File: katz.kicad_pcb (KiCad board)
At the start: 2 copper layers, 184.5 x 68.8 mm, 62 parts, among them SW1 choc_SW_HS, SW10 choc_SW_HS, SW11 choc_SW_HS, SW12 choc_SW_HS, SW13 choc_SW_HS, SW14 choc_SW_HS, SW15 choc_SW_HS, SW16 choc_SW_HS, SW17 choc_SW_HS, SW18 choc_SW_HS, SW19 choc_SW_HS, SW2 choc_SW_HS, SW20 choc_SW_HS, SW21 choc_SW_HS, SW22 choc_SW_HS, SW23 choc_SW_HS, SW24 choc_SW_HS, SW25 choc_SW_HS, SW26 choc_SW_HS, SW27 choc_SW_HS, SW28 choc_SW_HS, SW29 choc_SW_HS, SW3 choc_SW_HS, SW30 choc_SW_HS, SW4 choc_SW_HS, SW5 choc_SW_HS, SW6 choc_SW_HS, SW7 choc_SW_HS, SW8 choc_SW_HS, SW9 choc_SW_HS, U1 SeeeduinoXIAO

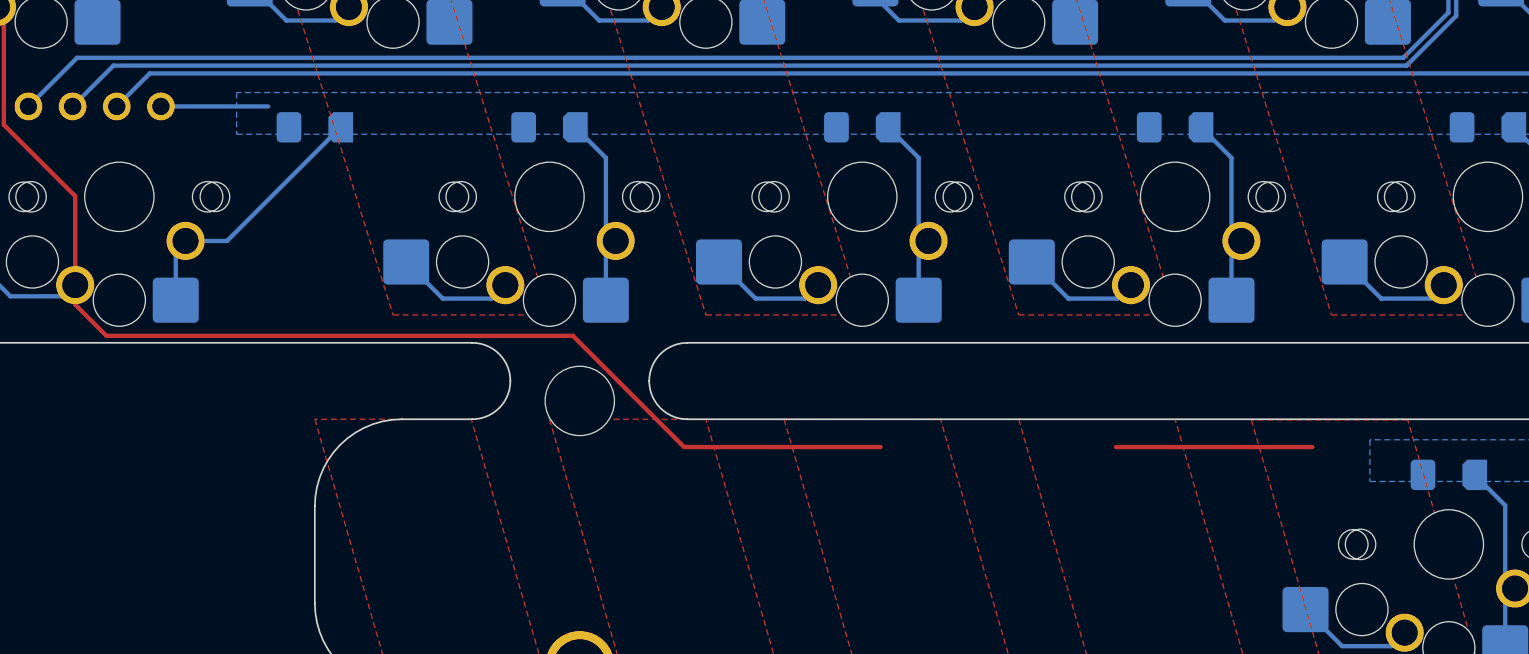
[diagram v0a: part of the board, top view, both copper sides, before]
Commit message: add pins to removable space bar
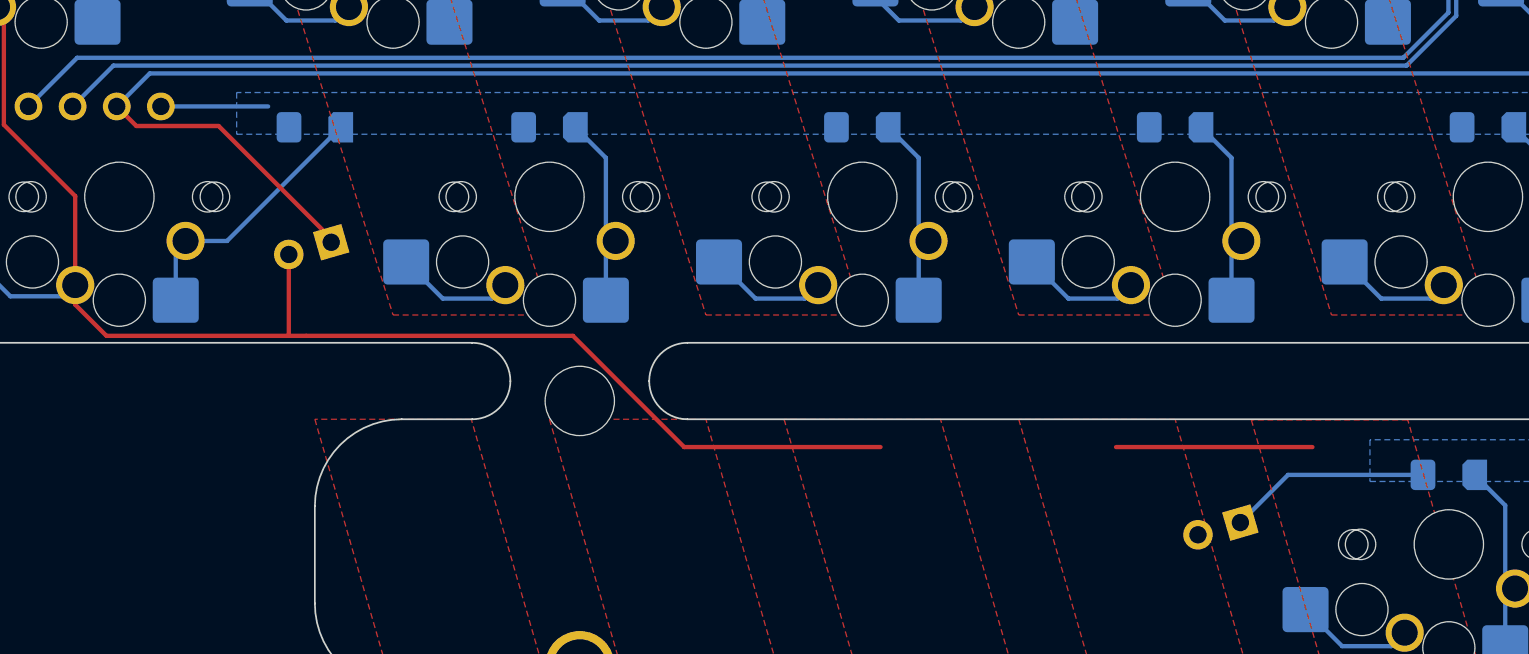
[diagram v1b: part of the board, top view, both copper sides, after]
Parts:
- added J1: modular spacebar, Connector_PinHeader_2.54mm:PinHeader_2x01_P2.54mm_Vertical, F.Cu at (129.8, 114.7)
- added J2: connector for modular spacebar, Connector_PinHeader_2.54mm:PinHeader_2x01_P2.54mm_Vertical, F.Cu at (77.4, 98.6)
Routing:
- net r6: track 117.0 -> 144.3 mm
- net c1: track 327.2 -> 331.9 mm

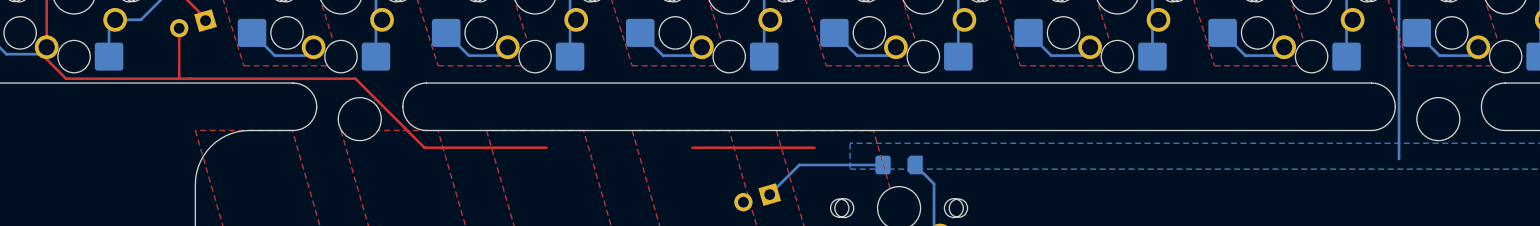
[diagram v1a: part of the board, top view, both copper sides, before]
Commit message: add break-off cuts to space bar
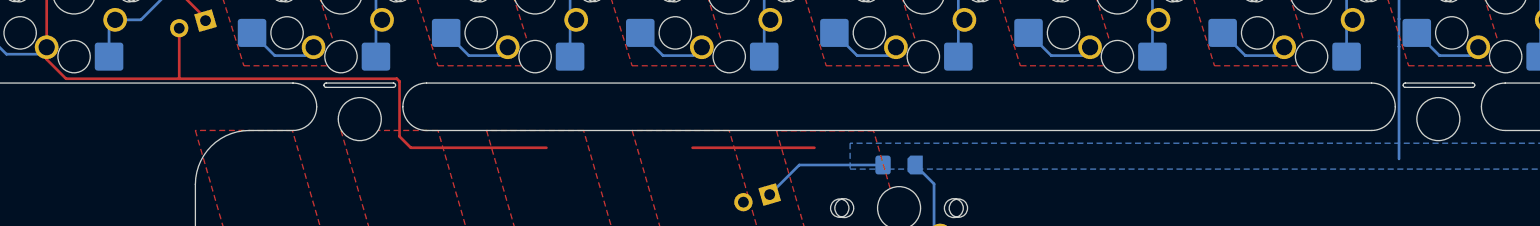
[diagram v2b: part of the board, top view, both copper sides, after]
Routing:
- net c1: track 331.9 -> 334.8 mm
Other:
- outline, holes or cut-outs redrawn
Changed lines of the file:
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@@
     (fp_arc (start -46.63125 7.500001) (mid -46.777697 7.853554) (end -47.13125 8.000001)
       (stroke (width 0.05) (type solid)) (layer "Eco2.User"))
-    (fp_arc (start 46.63125 -5.499999) (mid 46.777693 -5.853571) (end 47.13125 -5.999999)
+    (fp_arc (start 46.63125 -5.499999) (mid 46.777699 -5.853535) (end 47.13125 -5.999999)
       (stroke (width 0.05) (type solid)) (layer "Eco2.User"))
-    (fp_arc (start 47.13125 8.000001) (mid 46.777729 7.853537) (end 46.63125 7.500001)
+    (fp_arc (start 47.13125 8.000001) (mid 46.777693 7.853543) (end 46.63125 7.500001)
       (stroke (width 0.05) (type solid)) (layer "Eco2.User"))
-    (fp_arc (start 52.880039 -5.999999) (mid 53.233567 -5.853539) (end 53.380039 -5.499999)
+    (fp_arc (start 52.880039 -5.999999) (mid 53.233602 -5.853545) (end 53.380039 -5.499999)
       (stroke (width 0.05) (type solid)) (layer "Eco2.User"))
-    (fp_arc (start 53.38125 7.500001) (mid 53.234806 7.853571) (end 52.88125 8.000001)
+    (fp_arc (start 53.38125 7.500001) (mid 53.2348 7.853536) (end 52.88125 8.000001)
       (stroke (width 0.05) (type solid)) (layer "Eco2.User"))
     (pad "" thru_hole circle (at -50.00625 -6.985 180) (size 4 4) (drill 3.048) (layers "*.Cu" "B.Mask"))
@@
     )
   )
+  (gr_arc (start 95.0625 104.6) (mid 95.003921 104.741421) (end 94.8625 104.8)
+    (stroke (width 0.1) (type default)) (layer "Edge.Cuts"))
   (gr_line (start 185.562 108.8) (end 97.938 108.8)
     (stroke (width 0.1) (type default)) (layer "Edge.Cuts"))
@@
   (gr_arc (start 229 55.6) (mid 232.535534 57.064466) (end 234 60.6)
     (stroke (width 0.1) (type default)) (layer "Edge.Cuts"))
+  (gr_arc (start 188.4935 104.6) (mid 188.552079 104.458579) (end 188.6935 104.4)
+    (stroke (width 0.1) (type default)) (layer "Edge.Cuts"))
   (gr_arc (start 54.5 104.4) (mid 50.964466 102.935534) (end 49.5 99.4)
     (stroke (width 0.1) (type default)) (layer "Edge.Cuts"))
@@
   (gr_line (start 81.5 108.8) (end 85.55 108.8)
     (stroke (width 0.1) (type default)) (layer "Edge.Cuts"))
+  (gr_arc (start 94.8625 104.4) (mid 95.003921 104.458579) (end 95.0625 104.6)
+    (stroke (width 0.1) (type default)) (layer "Edge.Cuts"))
   (gr_line (start 54.5 55.6) (end 229 55.6)
     (stroke (width 0.1) (type default)) (layer "Edge.Cuts"))
@@
   (gr_line (start 234 60.6) (end 234 99.4)
     (stroke (width 0.1) (type default)) (layer "Edge.Cuts"))
+  (gr_arc (start 195.1315 104.6) (mid 195.072921 104.741421) (end 194.9315 104.8)
+    (stroke (width 0.1) (type default)) (layer "Edge.Cuts"))
+  (gr_arc (start 88.4245 104.6) (mid 88.483079 104.458579) (end 88.6245 104.4)
+    (stroke (width 0.1) (type default)) (layer "Edge.Cuts"))
   (gr_line (start 195.75 106.6) (end 195.75 106.6)
     (stroke (width 0.1) (type default)) (layer "Edge.Cuts"))
+  (gr_line (start 188.6935 104.4) (end 194.9315 104.4)
+    (stroke (width 0.1) (type default)) (layer "Edge.Cuts"))
   (gr_line (start 87.75 106.6) (end 87.75 106.6)
     (stroke (width 0.1) (type default)) (layer "Edge.Cuts"))
+  (gr_line (start 88.6245 104.4) (end 94.8625 104.4)
+    (stroke (width 0.1) (type default)) (layer "Edge.Cuts"))
   (gr_line (start 185.562 104.4) (end 97.938 104.4)
     (stroke (width 0.1) (type default)) (layer "Edge.Cuts"))
   (gr_arc (start 76.5 113.8) (mid 77.964466 110.264466) (end 81.5 108.8)
     (stroke (width 0.1) (type default)) (layer "Edge.Cuts"))
+  (gr_arc (start 88.6245 104.8) (mid 88.483079 104.741421) (end 88.4245 104.6)
+    (stroke (width 0.1) (type default)) (layer "Edge.Cuts"))
   (gr_arc (start 81.5 124.4) (mid 77.964466 122.935534) (end 76.5 119.4)
     (stroke (width 0.1) (type default)) (layer "Edge.Cuts"))
   (gr_line (start 202 124.4) (end 81.5 124.4)
     (stroke (width 0.1) (type default)) (layer "Edge.Cuts"))
+  (gr_line (start 194.9315 104.8) (end 188.6935 104.8)
+    (stroke (width 0.1) (type default)) (layer "Edge.Cuts"))
+  (gr_arc (start 188.6935 104.8) (mid 188.552079 104.741421) (end 188.4935 104.6)
+    (stroke (width 0.1) (type default)) (layer "Edge.Cuts"))
   (gr_arc (start 95.738 106.6) (mid 96.382365 105.044365) (end 97.938 104.4)
     (stroke (width 0.1) (type default)) (layer "Edge.Cuts"))
+  (gr_line (start 94.8625 104.8) (end 88.6245 104.8)
+    (stroke (width 0.1) (type default)) (layer "Edge.Cuts"))
   (gr_arc (start 187.762 106.6) (mid 187.117635 108.155635) (end 185.562 108.8)
     (stroke (width 0.1) (type default)) (layer "Edge.Cuts"))
+  (gr_arc (start 194.9315 104.4) (mid 195.072921 104.458579) (end 195.1315 104.6)
+    (stroke (width 0.1) (type default)) (layer "Edge.Cuts"))
   (gr_line (start 229 104.4) (end 197.95 104.4)
     (stroke (width 0.1) (type default)) (layer "Edge.Cuts"))
@@
   (segment (start 223.745 93.7575) (end 223.745 101.95) (width 0.25) (layer "B.Cu") (net 35))
   (segment (start 221.9875 92) (end 223.745 93.7575) (width 0.25) (layer "B.Cu") (net 35))
+  (segment (start 64.506928 104) (end 95.18 104) (width 0.25) (layer "F.Cu") (net 36))
   (segment (start 113.59944 123.2) (end 124.900559 123.2) (width 0.25) (layer "F.Cu") (net 36))
   (segment (start 64.025 67.975) (end 71.725 60.275) (width 0.25) (layer "F.Cu") (net 36))
   (segment (start 57.065 67.975) (end 64.025 67.975) (width 0.25) (layer "F.Cu") (net 36))
+  (segment (start 95.43 104.25) (end 95.43 109.35) (width 0.25) (layer "F.Cu") (net 36))
+  (segment (start 62.71 101.08) (end 62.71 102.203072) (width 0.25) (layer "F.Cu") (net 36))
   (segment (start 215.975 60.275) (end 220.21 64.51) (width 0.25) (layer "F.Cu") (net 36))
   (segment (start 58.60496 91.85496) (end 62.71 95.96) (width 0.25) (layer "F.Cu") (net 36))
   (segment (start 122.59944 110.4) (end 133.900559 110.4) (width 0.25) (layer "F.Cu") (net 36))
-  (segment (start 64.506928 104) (end 76 104) (width 0.25) (layer "F.Cu") (net 36))
   (segment (start 55.96 69.08) (end 57.065 67.975) (width 0.25) (layer "F.Cu") (net 36))
-  (segment (start 97.748881 110.4) (end 109.05 110.4) (width 0.25) (layer "F.Cu") (net 36))
-  (segment (start 91.348881 104) (end 97.748881 110.4) (width 0.25) (layer "F.Cu") (net 36))
-  (segment (start 62.71 102.203072) (end 64.506928 104) (width 0.25) (layer "F.Cu") (net 36))
   (segment (start 58.60496 85.47496) (end 58.60496 91.85496) (width 0.25) (layer "F.Cu") (net 36))
   (segment (start 53.19996 75.55999) (end 58.21 80.57003) (width 0.25) (layer "F.Cu") (net 36))
+  (segment (start 62.71 102.203072) (end 64.506928 104) (width 0.25) (layer "F.Cu") (net 36))
+  (segment (start 95.18 104) (end 95.43 104.25) (width 0.25) (layer "F.Cu") (net 36))
   (segment (start 58.21 80.57003) (end 58.21 85.08) (width 0.25) (layer "F.Cu") (net 36))
   (segment (start 52.39996 72.64004) (end 52.39996 75.55999) (width 0.25) (layer "F.Cu") (net 36))
-  (segment (start 76 104) (end 91.348881 104) (width 0.25) (layer "F.Cu") (net 36))
-  (segment (start 62.71 101.08) (end 62.71 102.203072) (width 0.25) (layer "F.Cu") (net 36))
   (segment (start 220.21 64.51) (end 220.21 69.08) (width 0.25) (layer "F.Cu") (net 36))
   (segment (start 71.725 60.275) (end 215.975 60.275) (width 0.25) (layer "F.Cu") (net 36))
@@
   (segment (start 74.999915 99.318631) (end 75 99.318716) (width 0.25) (layer "F.Cu") (net 36))
   (segment (start 75 99.318716) (end 75 104) (width 0.25) (layer "F.Cu") (net 36))
+  (segment (start 95.43 109.35) (end 96.48 110.4) (width 0.25) (layer "F.Cu") (net 36))
+  (segment (start 96.48 110.4) (end 109.05 110.4) (width 0.25) (layer "F.Cu") (net 36))
   (segment (start 52.39996 75.55999) (end 53.19996 75.55999) (width 0.25) (layer "F.Cu") (net 36))
   (segment (start 55.96 69.08) (end 52.39996 72.64004) (width 0.25) (layer "F.Cu") (net 36))
